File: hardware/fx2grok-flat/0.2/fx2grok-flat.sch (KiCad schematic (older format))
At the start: 36 parts, among them IC1 CY7C68013A-56, J1 Conn_02x05_Odd_Even, P1 pkl_USB_OTG, U1 3.3V, U2 USBLC6-2, U3 IP425x-4-TTL, U4 IP425x-4-TTL, U5 24LC00, U6 IP425x-4-TTL, X1 24MHz

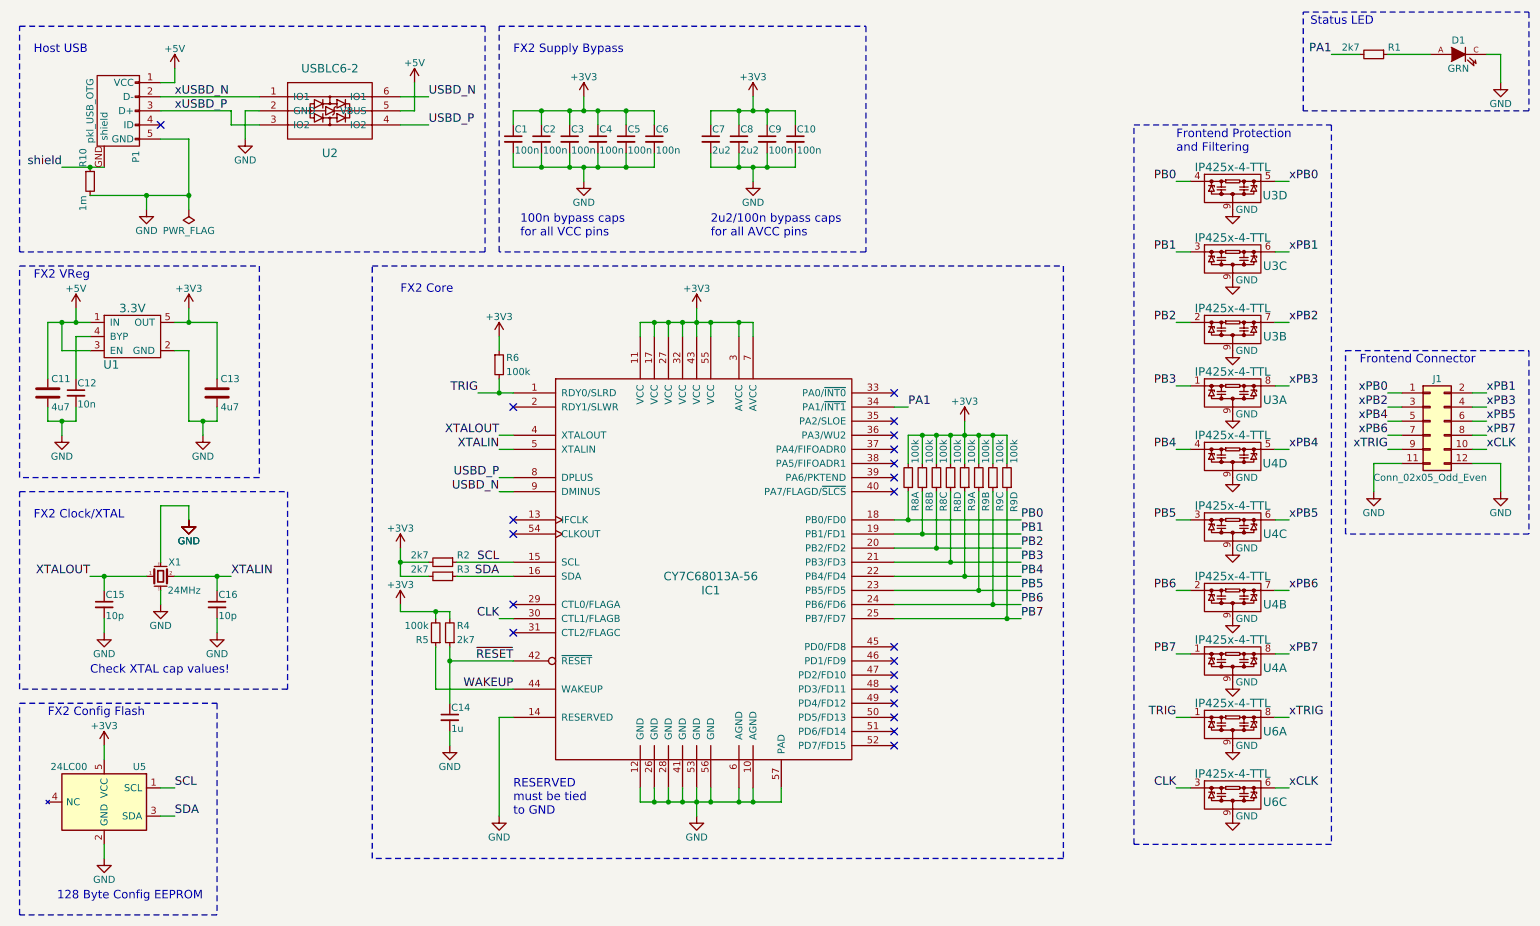
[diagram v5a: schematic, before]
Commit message: Minor value adjustment.
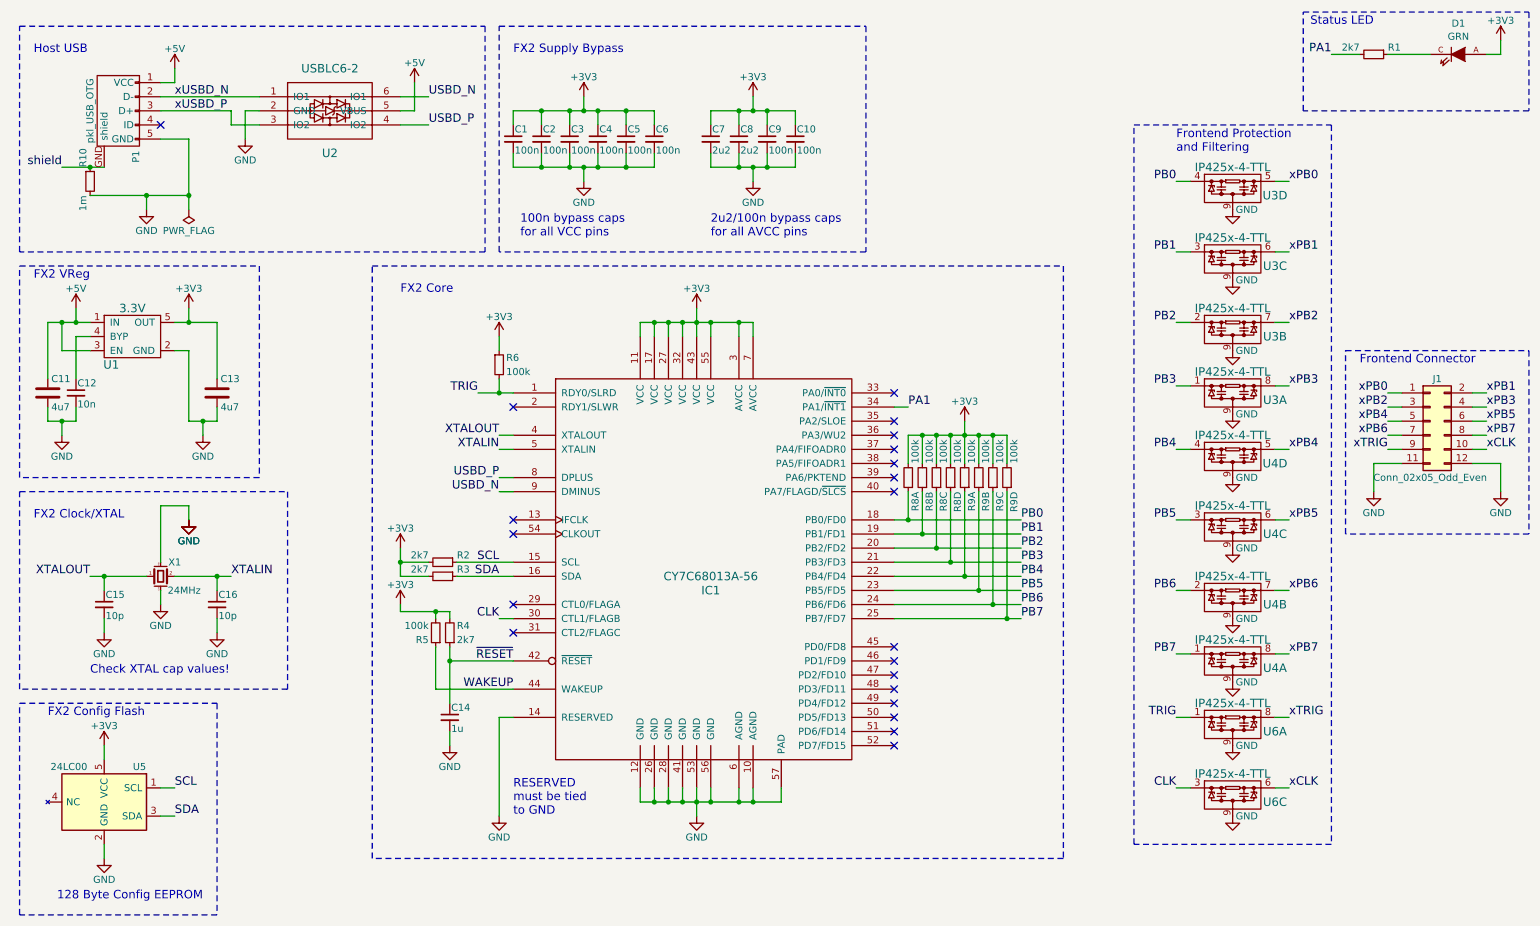
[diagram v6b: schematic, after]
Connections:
- net +3V3: now also D1.A
- net GND: no longer D1.C
- net at R1.1: now also D1.C; no longer D1.A
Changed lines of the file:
@@
-EESchema Schematic File Version 2
+EESchema Schematic File Version 4
 LIBS:power
 LIBS:device
@@
 LIBS:pkl_texas
 LIBS:fx2grok-flat-cache
-EELAYER 25 0
+EELAYER 26 0
 EELAYER END
 $Descr A4 11693 8268
@@
 	4900 2800 4900 2700
 Wire Wire Line
-	4900 2700 5700 2700
+	4900 2700 5000 2700
 Wire Wire Line
 	5700 2700 5700 2800
@@
 Connection ~ 5400 2700
 Wire Wire Line
-	5300 2600 5300 2800
+	5300 2600 5300 2700
 Connection ~ 5300 2700
 Wire Wire Line
@@
 PA1
 Wire Wire Line
-	6700 4100 7600 4100
-Wire Wire Line
-	6700 4200 7600 4200
-Wire Wire Line
-	6700 4300 7600 4300
-Wire Wire Line
-	6700 4400 7600 4400
-Wire Wire Line
-	6700 4500 7600 4500
-Wire Wire Line
-	6700 4600 7600 4600
-Wire Wire Line
-	6700 4700 7600 4700
-Wire Wire Line
-	6700 4800 7600 4800
+	6700 4100 6800 4100
+Wire Wire Line
+	6700 4200 6900 4200
+Wire Wire Line
+	6700 4300 7000 4300
+Wire Wire Line
+	6700 4400 7100 4400
+Wire Wire Line
+	6700 4500 7200 4500
+Wire Wire Line
+	6700 4600 7300 4600
+Wire Wire Line
+	6700 4700 7400 4700
+Wire Wire Line
+	6700 4800 7500 4800
 Text Label 7600 4100 0    60   ~ 0
 PB0
@@
 	3400 4400 3200 4400
 Wire Wire Line
-	3200 4300 3200 4500
+	3200 4300 3200 4400
 Wire Wire Line
 	3200 4500 3400 4500
@@
 	4900 6000 4900 6100
 Wire Wire Line
-	4900 6100 5900 6100
+	4900 6100 5000 6100
 Wire Wire Line
 	5700 6100 5700 6000
@@
 Connection ~ 5400 6100
 Wire Wire Line
-	5300 6000 5300 6200
+	5300 6000 5300 6100
 Connection ~ 5300 6100
 Wire Wire Line
@@
 U 1 1 59BC9087
 P 10700 800
-F 0 "D1" H 10700 900 50  0000 C CNN
-F 1 "GRN" H 10700 700 50  0000 C CNN
+F 0 "D1" H 10700 1020 50  0000 C CNN
+F 1 "GRN" H 10700 927 50  0000 C CNN
 F 2 "pkl_dipol:D_0603" H 10700 800 60  0001 C CNN
 F 3 "" H 10700 800 60  0000 C CNN
@@
 F 5 "ANY" H 10700 800 60  0001 C CNN "Source"
 	1    10700 800
-	1    0    0    -1
+	-1   0    0    -1
 $EndComp
 $Comp
@@
 	10900 800  11000 800
 Wire Wire Line
-	11000 800  11000 1000
-$Comp
-L GND #PWR07
-U 1 1 59BC94B6
-P 11000 1000
-F 0 "#PWR07" H 11000 750 50  0001 C CNN
-F 1 "GND" H 11000 850 50  0000 C CNN
-F 2 "" H 11000 1000 50  0001 C CNN
-F 3 "" H 11000 1000 50  0001 C CNN
-	1    11000 1000
-	1    0    0    -1
-$EndComp
+	11000 800  11000 700
 Wire Wire Line
 	1600 1000 1600 900
@@
 	1500 1400 1700 1400
 Wire Wire Line
-	1700 1400 1700 1900
-Wire Wire Line
-	1000 1800 1700 1800
+	1700 1400 1700 1800
+Wire Wire Line
+	1000 1800 1400 1800
 Wire Wire Line
 	1400 1800 1400 1900
@@
 $EndComp
 Wire Wire Line
-	700  2700 1000 2700
+	700  2700 800  2700
 Wire Wire Line
 	1500 1000 1600 1000
@@
 	700  3300 700  3400
 Wire Wire Line
-	700  3400 900  3400
+	700  3400 800  3400
 Wire Wire Line
 	900  3400 900  3300
@@
 $EndComp
 Wire Wire Line
-	1600 2700 1900 2700
+	1600 2700 1700 2700
 Wire Wire Line
 	1900 2700 1900 3100
@@
 	1900 3400 1900 3300
 Wire Wire Line
-	1700 3400 1900 3400
+	1700 3400 1800 3400
 Wire Wire Line
 	1800 3400 1800 3500
@@
 	4000 1300 4000 1200
 Wire Wire Line
-	4000 1200 5000 1200
+	4000 1200 4200 1200
 Wire Wire Line
 	5000 1200 5000 1300
@@
 	4000 1500 4000 1600
 Wire Wire Line
-	4000 1600 5000 1600
+	4000 1600 4200 1600
 Wire Wire Line
 	5000 1600 5000 1500
@@
 	5400 1300 5400 1200
 Wire Wire Line
-	5400 1200 6000 1200
+	5400 1200 5600 1200
 Wire Wire Line
 	6000 1200 6000 1300
@@
 	5400 1500 5400 1600
 Wire Wire Line
-	5400 1600 6000 1600
+	5400 1600 5600 1600
 Wire Wire Line
 	6000 1600 6000 1500
@@
 $EndComp
 Wire Wire Line
-	1600 4500 2000 4500
-Wire Wire Line
-	1000 4500 1400 4500
+	1600 4500 1900 4500
+Wire Wire Line
+	1000 4500 1100 4500
 Wire Wire Line
 	1900 4500 1900 4600
@@
 	6800 3700 6800 3500
 Wire Wire Line
-	6800 3500 7500 3500
+	6800 3500 6900 3500
 Wire Wire Line
 	7500 3500 7500 3700
@@
 Connection ~ 7300 3500
 Wire Wire Line
-	7200 3400 7200 3700
+	7200 3400 7200 3500
 Connection ~ 7200 3500
 Wire Wire Line
@@
 $EndComp
 Wire Wire Line
-	800  1600 1100 1600
+	800  1600 1000 1600
 Connection ~ 1000 1600
 Text Label 800  1600 2    60   ~ 0
@@
 Connection ~ 5700 6100
 Wire Wire Line
-	3750 3200 4000 3200
+	3750 3200 3900 3200
 Text Label 3750 3200 2    60   ~ 0
 TRIG
@@
 	3000 6500 3000 2300
 Wire Wire Line
-	3550 5000 3550 5400
+	3550 5000 3550 5100
 Wire Wire Line
 	3200 4700 3200 4750
 Wire Wire Line
-	3200 4750 3550 4750
+	3200 4750 3450 4750
 Wire Wire Line
 	3550 4750 3550 4800
@@
 Text Notes 1800 6800 2    60   ~ 0
 128 Byte Config EEPROM
+Wire Wire Line
+	5600 2700 5700 2700
+Wire Wire Line
+	5400 2700 5600 2700
+Wire Wire Line
+	5300 2700 5400 2700
+Wire Wire Line
+	5300 2700 5300 2800
+Wire Wire Line
+	5200 2700 5300 2700
+Wire Wire Line
+	5100 2700 5200 2700
+Wire Wire Line
+	5000 2700 5100 2700
+Wire Wire Line
+	3200 4400 3200 4500
+Wire Wire Line
+	5600 6100 5700 6100
+Wire Wire Line
+	5400 6100 5600 6100
+Wire Wire Line
+	5300 6100 5400 6100
+Wire Wire Line
+	5300 6100 5300 6200
+Wire Wire Line
+	5200 6100 5300 6100
+Wire Wire Line
+	5100 6100 5200 6100
+Wire Wire Line
+	5000 6100 5100 6100
+Wire Wire Line
+	1400 1800 1700 1800
+Wire Wire Line
+	800  3400 900  3400
+Wire Wire Line
+	1800 3400 1900 3400
+Wire Wire Line
+	900  2700 1000 2700
+Wire Wire Line
+	1700 2700 1900 2700
+Wire Wire Line
+	800  2700 900  2700
+Wire Wire Line
+	4800 1200 5000 1200
+Wire Wire Line
+	4600 1200 4800 1200
+Wire Wire Line
+	4400 1200 4500 1200
+Wire Wire Line
+	4200 1200 4400 1200
+Wire Wire Line
+	4200 1600 4400 1600
+Wire Wire Line
+	4400 1600 4500 1600
+Wire Wire Line
+	4600 1600 4800 1600
+Wire Wire Line
+	4800 1600 5000 1600
+Wire Wire Line
+	4500 1200 4600 1200
+Wire Wire Line
+	4500 1600 4600 1600
+Wire Wire Line
+	5800 1200 6000 1200
+Wire Wire Line
+	5600 1200 5700 1200
+Wire Wire Line
+	5800 1600 6000 1600
+Wire Wire Line
+	5600 1600 5700 1600
+Wire Wire Line
+	5700 1600 5800 1600
+Wire Wire Line
+	5700 1200 5800 1200
+Wire Wire Line
+	1900 4500 2000 4500
+Wire Wire Line
+	1100 4500 1400 4500
+Wire Wire Line
+	7400 3500 7500 3500
+Wire Wire Line
+	7300 3500 7400 3500
+Wire Wire Line
+	7200 3500 7300 3500
+Wire Wire Line
+	7200 3500 7200 3700
+Wire Wire Line
+	7100 3500 7200 3500
+Wire Wire Line
+	7000 3500 7100 3500
+Wire Wire Line
+	6900 3500 7000 3500
+Wire Wire Line
+	7300 4600 7600 4600
+Wire Wire Line
+	7400 4700 7600 4700
+Wire Wire Line
+	7500 4800 7600 4800
+Wire Wire Line
+	1700 1800 1700 1900
+Wire Wire Line
+	1000 1600 1100 1600
+Wire Wire Line
+	5700 6100 5900 6100
+Wire Wire Line
+	7200 4500 7600 4500
+Wire Wire Line
+	7100 4400 7600 4400
+Wire Wire Line
+	7000 4300 7600 4300
+Wire Wire Line
+	6900 4200 7600 4200
+Wire Wire Line
+	6800 4100 7600 4100
+Wire Wire Line
+	3900 3200 4000 3200
+Wire Wire Line
+	3450 4750 3550 4750
+Wire Wire Line
+	3550 5100 3550 5400
+$Comp
+L +3V3 #PWR?
+U 1 1 5A2DF8E7
+P 11000 700
+F 0 "#PWR?" H 11000 550 50  0001 C CNN
+F 1 "+3V3" H 11000 840 50  0000 C CNN
+F 2 "" H 11000 700 50  0001 C CNN
+F 3 "" H 11000 700 50  0001 C CNN
+	1    11000 700
+	1    0    0    -1
+$EndComp
 $EndSCHEMATC
